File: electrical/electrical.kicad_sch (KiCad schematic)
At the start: 0 parts

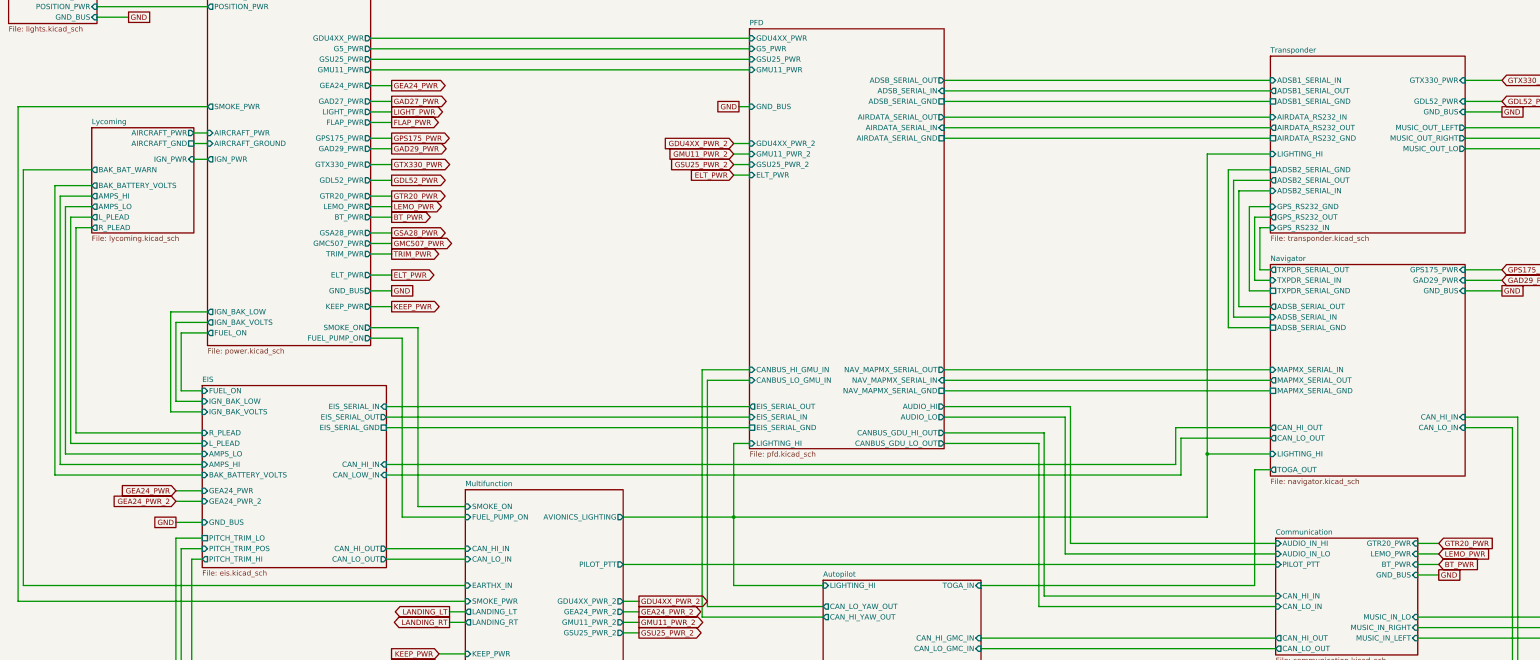
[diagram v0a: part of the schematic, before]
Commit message: Upgraded G3X Touch to Axis
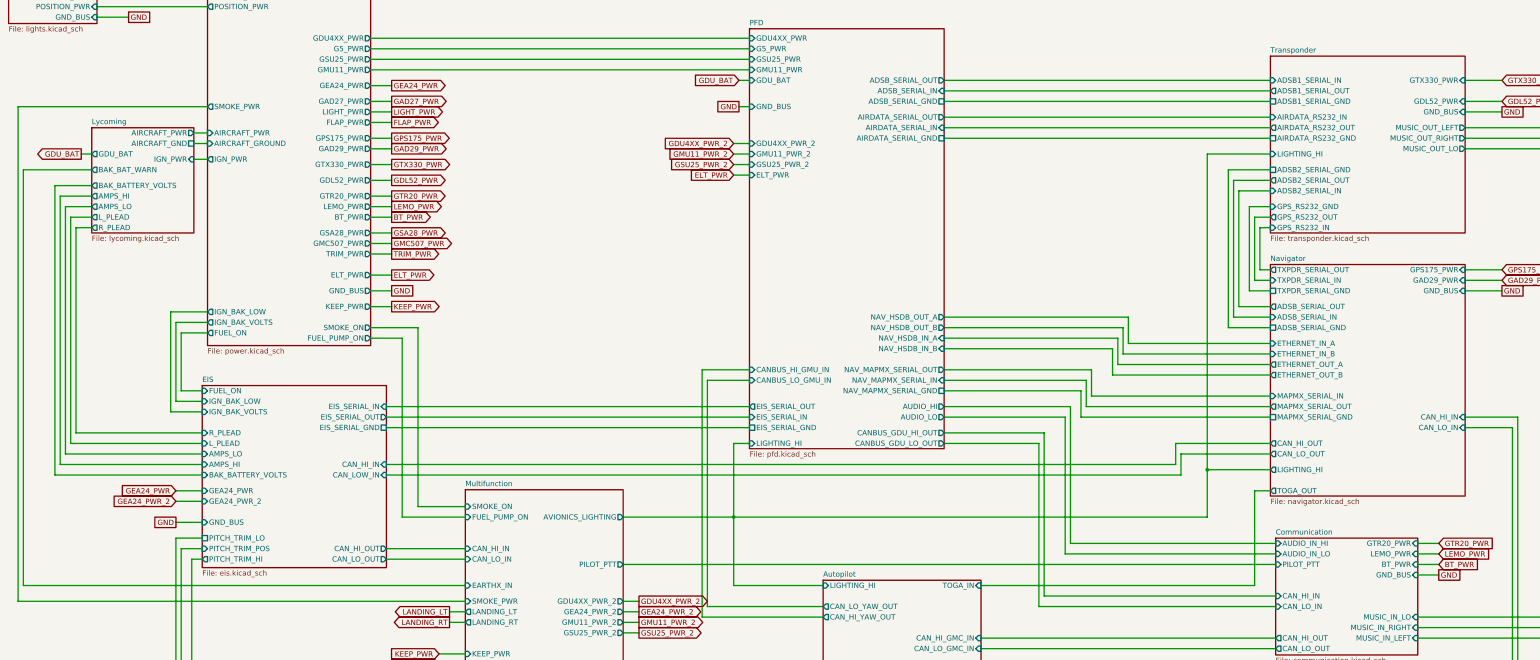
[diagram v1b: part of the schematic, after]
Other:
- sheet Lycoming ports: added GDU_BAT; removed none
- sheet Navigator ports: added ETHERNET_IN_A, ETHERNET_IN_B, ETHERNET_OUT_A, ETHERNET_OUT_B; removed none
- sheet PFD ports: added GDU_BAT, NAV_HSDB_IN_A, NAV_HSDB_IN_B, NAV_HSDB_OUT_A, NAV_HSDB_OUT_B; removed none
